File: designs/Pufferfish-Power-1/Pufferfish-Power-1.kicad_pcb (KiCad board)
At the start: 2 copper layers, 9 parts, among them Q1 BSC028N06LS3, Q2 BSC028N06LS3, Q3 BSC028N06LS3, Q4 BSC028N06LS3, U1 LTC4421IUHE

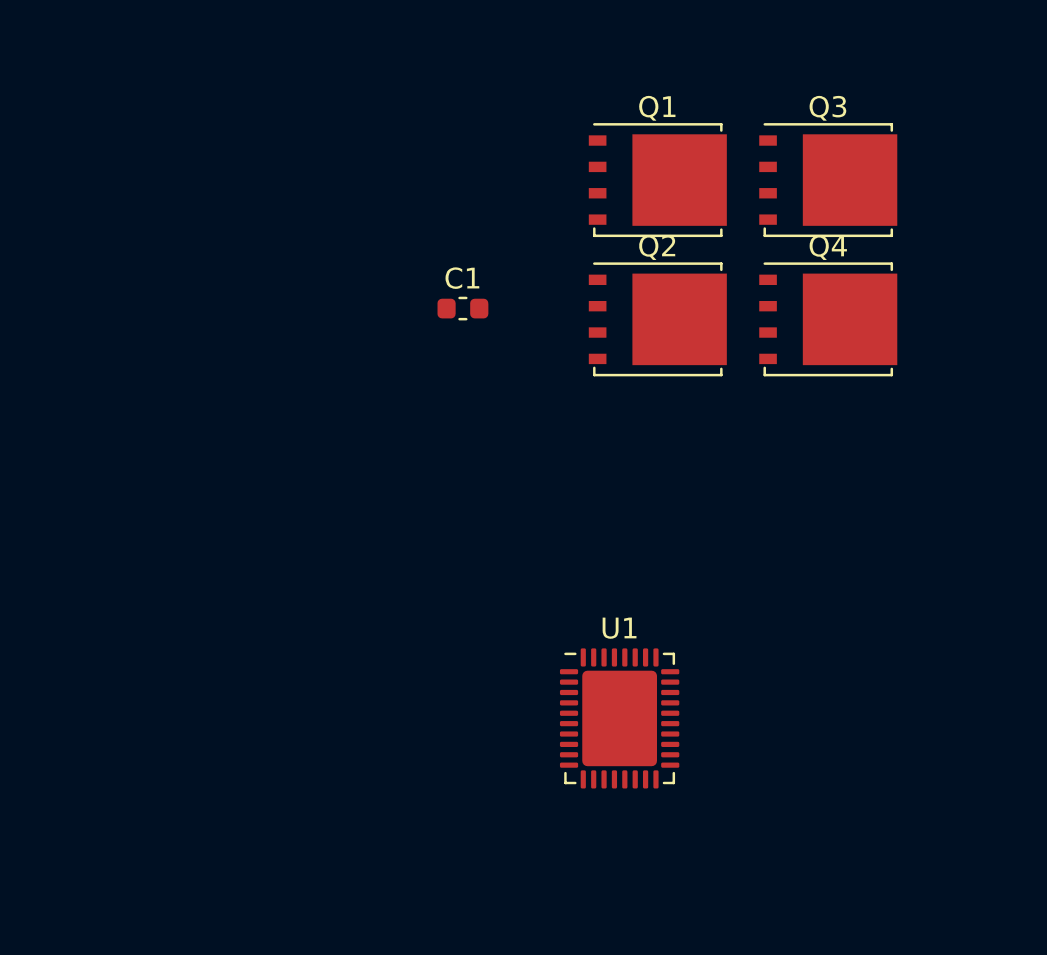
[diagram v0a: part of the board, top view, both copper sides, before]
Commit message: - Updated thresholds for LTC4421 circuit - Added inputs page - Added passives to library
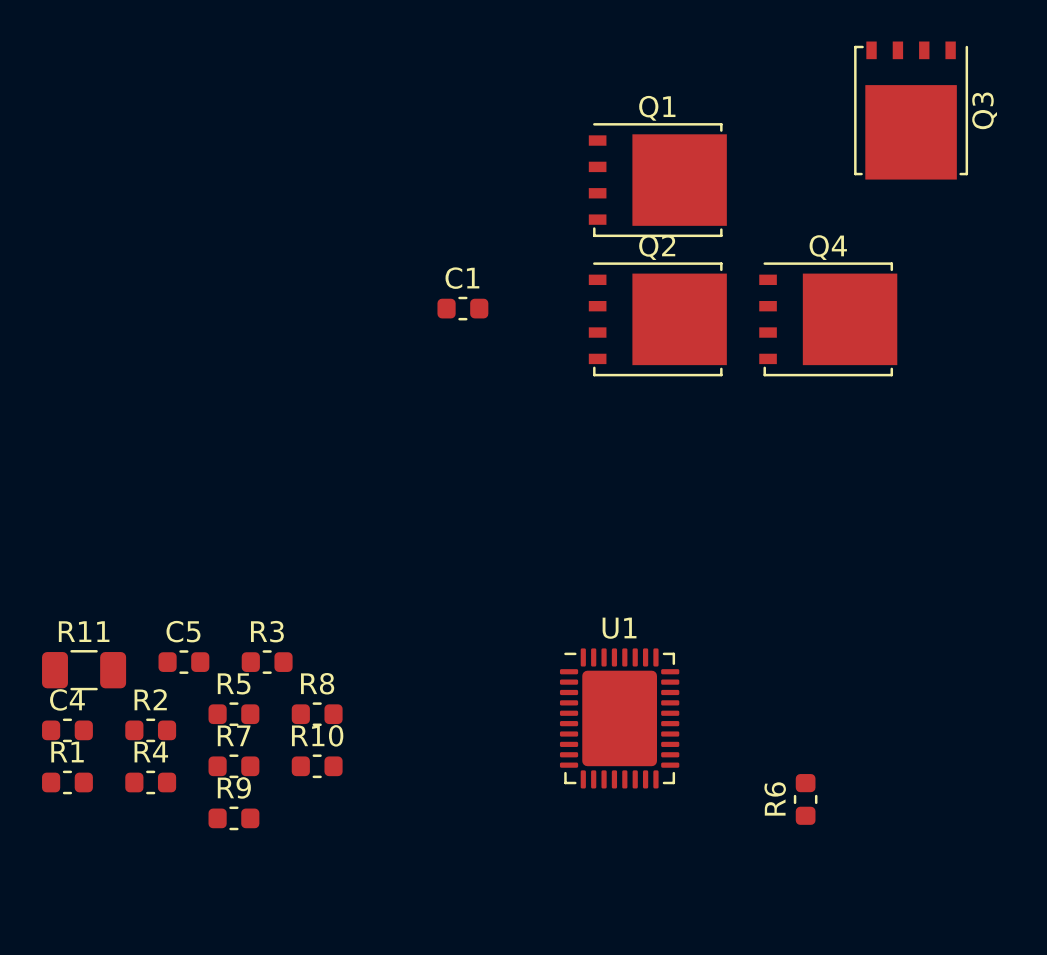
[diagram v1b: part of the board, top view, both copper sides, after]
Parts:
- added C4: CAP_33nF_25V_X7R_0603, Pufferfish:CAP_SMD_0603, F.Cu at (105.4, 114.3)
- added C5: CAP_33nF_25V_X7R_0603, Pufferfish:CAP_SMD_0603, F.Cu at (111.0, 111.0)
- added R1: RES_768K_0603_SMD, Pufferfish:RES_SMD_0603, F.Cu at (105.4, 116.8)
- added R10: RES_47K_0603_SMD, Pufferfish:RES_SMD_0603, F.Cu at (117.4, 116.0)
- added R11: CSNL1206FT3L00, Pufferfish:RES_SMD_1206, F.Cu at (106.2, 111.4)
- added R2: RES_24K9_0603_SMD, Pufferfish:RES_SMD_0603, F.Cu at (109.4, 114.3)
- added R3: RES_750K_0603_SMD, Pufferfish:RES_SMD_0603, F.Cu at (115.0, 111.0)
- added R4: RES_10K_0603_SMD, Pufferfish:RES_SMD_0603, F.Cu at (109.4, 116.8)
- added R5: RES_47K_0603_SMD, Pufferfish:RES_SMD_0603, F.Cu at (113.4, 113.5)
- added R6: RES_768K_0603_SMD, Pufferfish:RES_SMD_0603, F.Cu at (141.0, 117.6)
- added R7: RES_24K9_0603_SMD, Pufferfish:RES_SMD_0603, F.Cu at (113.4, 116.0)
- added R8: RES_750K_0603_SMD, Pufferfish:RES_SMD_0603, F.Cu at (117.4, 113.5)
- added R9: RES_10K_0603_SMD, Pufferfish:RES_SMD_0603, F.Cu at (113.4, 118.5)
- moved Q3 5.21 mm to (146.1, 84.4), turned to 270 degrees
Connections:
- net Net-(Q1-Pad1) renamed VIN-PRIMARY-12V0
- U1 pad 22: Net-(U1-Pad22) -> /LTC4221/LTC4421-TMR2
- U1 pad 23: Net-(U1-Pad23) -> /LTC4221/LTC4421-OV2
- U1 pad 24: Net-(U1-Pad24) -> /LTC4221/LTC4421-UVR2
- U1 pad 25: Net-(U1-Pad25) -> /LTC4221/LTC4421-UVF2
- U1 pad 4: Net-(U1-Pad4) -> /LTC4221/LTC4421-UVF1
- U1 pad 5: Net-(U1-Pad5) -> /LTC4221/LTC4421-UVR1
- U1 pad 6: Net-(U1-Pad6) -> /LTC4221/LTC4421-OV1
- U1 pad 7: Net-(U1-Pad7) -> /LTC4221/LTC4421-TMR1

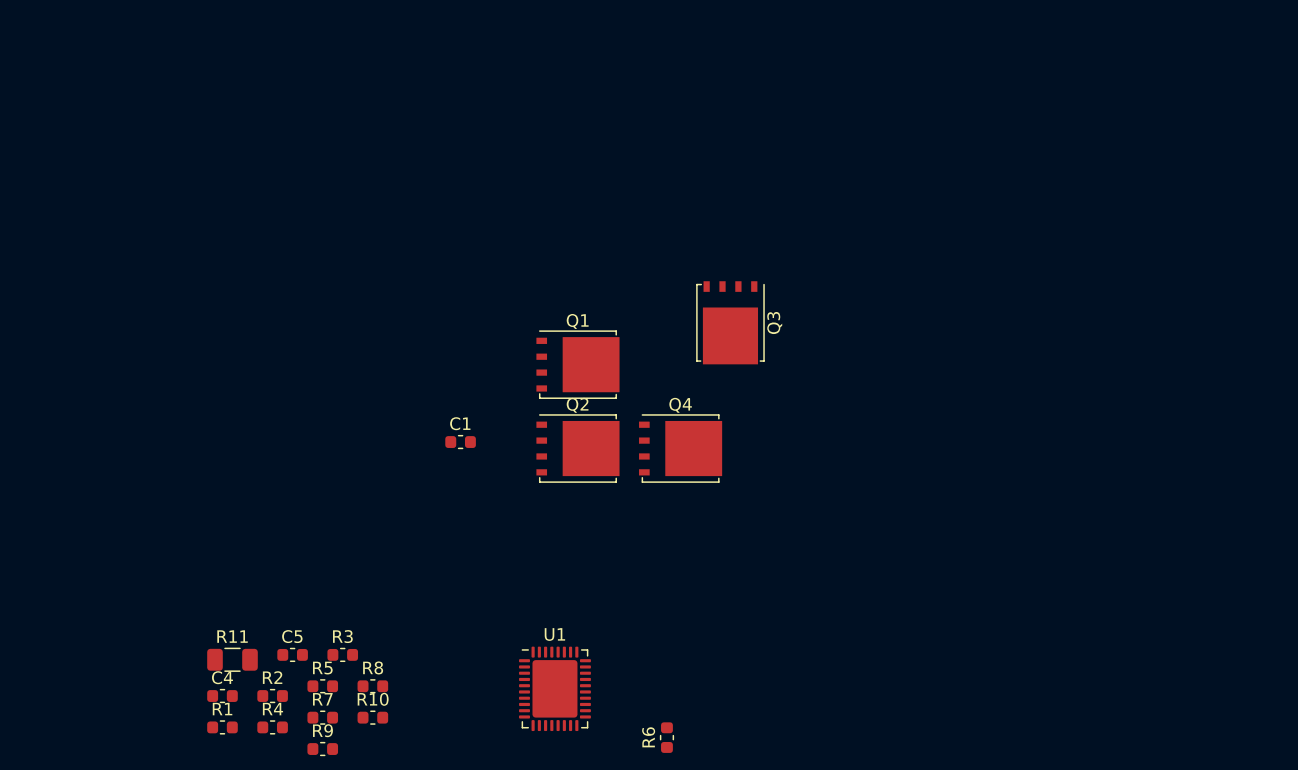
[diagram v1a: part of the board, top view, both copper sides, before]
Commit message: - Finished LTC4421 Design - Added Input power path - Updated libraries - Added pages for interface connectors and 24V Boost
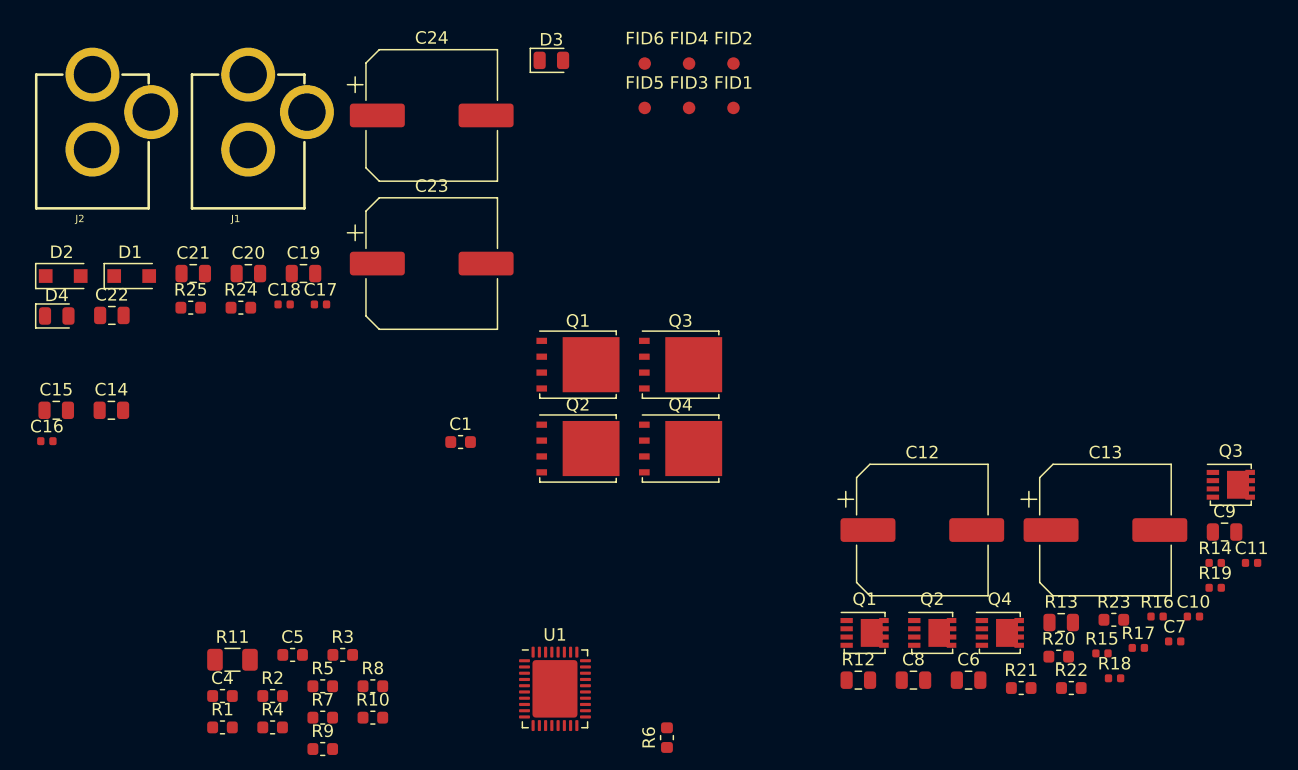
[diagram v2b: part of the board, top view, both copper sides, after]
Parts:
- added C10: CAP_47nF_50V_X7R_0402, Pufferfish:CAP_SMD_0402, F.Cu at (183.1, 107.9)
- added C11: CAP_100nF_50V_X7R_0402, Pufferfish:CAP_SMD_0402, F.Cu at (187.7, 103.7)
- added C12: CAP_AE_SMD_220uF_25V_8mm, Capacitor_SMD:CP_Elec_10x7.9, F.Cu at (161.4, 101.0)
- added C13: CAP_AE_SMD_220uF_25V_8mm, Capacitor_SMD:CP_Elec_10x7.9, F.Cu at (176.1, 101.0)
- added C14: CAP_10uF_35V_X5R_0805, Pufferfish:CAP_SMD_0805, F.Cu at (96.5, 91.4)
- added C15: CAP_10uF_35V_X5R_0805, Pufferfish:CAP_SMD_0805, F.Cu at (92.1, 91.4)
- added C16: CAP_100nF_50V_X7R_0402, Pufferfish:CAP_SMD_0402, F.Cu at (91.4, 93.9)
- added C17: CAP_100nF_50V_X7R_0402, Pufferfish:CAP_SMD_0402, F.Cu at (113.2, 83.0)
- added C18: CAP_100nF_50V_X7R_0402, Pufferfish:CAP_SMD_0402, F.Cu at (110.3, 83.0)
- added C19: CAP_10uF_35V_X5R_0805, Pufferfish:CAP_SMD_0805, F.Cu at (111.9, 80.5)
- added C20: CAP_10uF_35V_X5R_0805, Pufferfish:CAP_SMD_0805, F.Cu at (107.5, 80.5)
- added C21: CAP_10uF_35V_X5R_0805, Pufferfish:CAP_SMD_0805, F.Cu at (103.1, 80.5)
- added C22: CAP_10uF_35V_X5R_0805, Pufferfish:CAP_SMD_0805, F.Cu at (96.6, 83.8)
- added C23: CAP_AE_SMD_220uF_25V_8mm, Capacitor_SMD:CP_Elec_10x7.9, F.Cu at (122.2, 79.7)
- added C24: CAP_AE_SMD_220uF_25V_8mm, Capacitor_SMD:CP_Elec_10x7.9, F.Cu at (122.2, 67.8)
- added C6: CAP_10uF_35V_X5R_0805, Pufferfish:CAP_SMD_0805, F.Cu at (165.1, 113.0)
- added C7: CAP_47nF_50V_X7R_0402, Pufferfish:CAP_SMD_0402, F.Cu at (181.6, 109.9)
- added C8: CAP_10uF_35V_X5R_0805, Pufferfish:CAP_SMD_0805, F.Cu at (160.7, 113.0)
- added C9: CAP_10uF_35V_X5R_0805, Pufferfish:CAP_SMD_0805, F.Cu at (185.6, 101.2)
- added D1: TVS_15V_SOD123FL-2, Diode_SMD:D_SOD-123F, F.Cu at (98.1, 80.7)
- added D2: TVS_15V_SOD123FL-2, Diode_SMD:D_SOD-123F, F.Cu at (92.7, 80.7)
- added D3: LED_SMD_0805, Pufferfish:LED_SMD_0805, F.Cu at (131.7, 63.4)
- added D4: LED_SMD_0805, Pufferfish:LED_SMD_0805, F.Cu at (92.2, 83.9)
- added FID1: Fiducial, Fiducial:Fiducial_1mm_Mask2mm, F.Cu at (146.3, 67.2)
- added FID2: Fiducial, Fiducial:Fiducial_1mm_Mask2mm, F.Cu at (146.3, 63.7)
- added FID3: Fiducial, Fiducial:Fiducial_1mm_Mask2mm, F.Cu at (142.7, 67.2)
- added FID4: Fiducial, Fiducial:Fiducial_1mm_Mask2mm, F.Cu at (142.7, 63.7)
- added FID5: Fiducial, Fiducial:Fiducial_1mm_Mask2mm, F.Cu at (139.2, 67.2)
- added FID6: Fiducial, Fiducial:Fiducial_1mm_Mask2mm, F.Cu at (139.2, 63.7)
- added J1: POWER_JACK_PTH, Pufferfish:POWER_JACK_PTH, F.Cu at (107.5, 78.3)
- added J2: POWER_JACK_PTH, Pufferfish:POWER_JACK_PTH, F.Cu at (95.0, 78.3)
- added Q1: SiR158DP, Package_SO:Vishay_PowerPAK_1212-8_Single, F.Cu at (156.8, 109.2)
- added Q2: SiR158DP, Package_SO:Vishay_PowerPAK_1212-8_Single, F.Cu at (162.2, 109.2)
- added Q3: SiR158DP, Package_SO:Vishay_PowerPAK_1212-8_Single, F.Cu at (186.1, 97.4)
- added Q4: SiR158DP, Package_SO:Vishay_PowerPAK_1212-8_Single, F.Cu at (167.6, 109.2)
- added R12: RES_1R2_0805_SMD, Pufferfish:RES_SMD_0805, F.Cu at (156.3, 113.0)
- added R13: RES_1R2_0805_SMD, Pufferfish:RES_SMD_0805, F.Cu at (172.5, 108.4)
- added R14: RES_0R_0402_SMD, Pufferfish:RES_SMD_0402, F.Cu at (184.8, 103.7)
- added R15: RES_0R_0402_SMD, Pufferfish:RES_SMD_0402, F.Cu at (175.8, 110.9)
- added R16: RES_0R_0402_SMD, Pufferfish:RES_SMD_0402, F.Cu at (180.2, 107.9)
- added R17: RES_0R_0402_SMD, Pufferfish:RES_SMD_0402, F.Cu at (178.7, 110.5)
- added R18: RES_0R_0402_SMD, Pufferfish:RES_SMD_0402, F.Cu at (176.8, 112.9)
- added R19: RES_0R_0402_SMD, Pufferfish:RES_SMD_0402, F.Cu at (184.8, 105.6)
- added R20: RES_10K_0603_SMD, Pufferfish:RES_SMD_0603, F.Cu at (172.3, 111.2)
- added R21: RES_10K_0603_SMD, Pufferfish:RES_SMD_0603, F.Cu at (169.3, 113.7)
- added R22: RES_10K_0603_SMD, Pufferfish:RES_SMD_0603, F.Cu at (173.3, 113.7)
- added R23: RES_10K_0603_SMD, Pufferfish:RES_SMD_0603, F.Cu at (176.7, 108.2)
- added R24: RES_330R_0603_SMD, Pufferfish:RES_SMD_0603, F.Cu at (106.9, 83.2)
- added R25: RES_330R_0603_SMD, Pufferfish:RES_SMD_0603, F.Cu at (102.9, 83.2)
- moved Q3 5.21 mm to (142.1, 87.8), turned to 0 degrees
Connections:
- R11 pad 1: Net-(R11-Pad1) -> VSYS-12V0
- R11 pad 2: Net-(R11-Pad2) -> /LTC4221/LTC4421-SENSE
- U1 pad 1: Net-(U1-Pad1) -> /LTC4221/LTC4421-SRC1
- U1 pad 17: Net-(U1-Pad17) -> INTVCC-LTC4421
- U1 pad 2: Net-(U1-Pad2) -> /LTC4221/LTC4421-GATE1
- U1 pad 21: Net-(U1-Pad21) -> LTC4421-PWR-nDISABLE2
- U1 pad 26: Net-(U1-Pad26) -> VIN-BACKUP-12V0
- U1 pad 27: Net-(U1-Pad27) -> /LTC4221/LTC4421-SOURCE2
- U1 pad 28: Net-(U1-Pad28) -> /LTC4221/LTC4421-GATE2
- U1 pad 29: Net-(U1-Pad29) -> /LTC4221/LTC4421-SENSE
- U1 pad 3: Net-(U1-Pad3) -> VIN-PRIMARY-12V0
- U1 pad 30: Net-(U1-Pad30) -> VSYS-12V0
- U1 pad 32: Net-(U1-Pad32) -> VSYS-12V0
- U1 pad 33: Net-(U1-Pad33) -> VSYS-12V0
- U1 pad 34: Net-(U1-Pad34) -> VSYS-12V0
- U1 pad 35: Net-(U1-Pad35) -> VSYS-12V0
- U1 pad 36: Net-(U1-Pad36) -> /LTC4221/LTC4421-SENSE
- U1 pad 8: Net-(U1-Pad8) -> LTC4421-PWR-nDISABLE1

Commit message: - Added 3.3V and 5V Buck designs - Added interface connectors - Added voltage measurement circuit - Added preliminary charging circuit
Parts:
- added C25: CAP_22uF_25V_X5R_0805, Pufferfish:CAP_SMD_0805, F.Cu at (135.9, 38.1)
- added C26: CAP_22uF_25V_X5R_0805, Pufferfish:CAP_SMD_0805, F.Cu at (131.4, 42.6)
- added C27: CAP_22uF_25V_X5R_0805, Pufferfish:CAP_SMD_0805, F.Cu at (135.8, 44.0)
- added C28: CAP_22uF_25V_X5R_0805, Pufferfish:CAP_SMD_0805, F.Cu at (140.3, 38.1)
- added C29: CAP_22uF_25V_X5R_0805, Pufferfish:CAP_SMD_0805, F.Cu at (135.9, 41.0)
- added C30: CAP_22uF_25V_X5R_0805, Pufferfish:CAP_SMD_0805, F.Cu at (131.4, 45.6)
- added C31: CAP_22uF_25V_X5R_0805, Pufferfish:CAP_SMD_0805, F.Cu at (136.7, 24.0)
- added C32: CAP_22uF_25V_X5R_0805, Pufferfish:CAP_SMD_0805, F.Cu at (126.0, 29.2)
- added C33: CAP_22uF_25V_X5R_0805, Pufferfish:CAP_SMD_0805, F.Cu at (141.1, 21.0)
- added C34: CAP_10uF_35V_X5R_0805, Pufferfish:CAP_SMD_0805, F.Cu at (130.4, 32.1)
- added C35: CAP_4.7uF_16V_X6S_0603, Pufferfish:CAP_SMD_0603, F.Cu at (140.9, 23.8)
- added C36: CAP_100nF_50V_X7R_0402, Pufferfish:CAP_SMD_0402, F.Cu at (142.1, 26.0)
- added C37: CAP_100nF_50V_X7R_0402, Pufferfish:CAP_SMD_0402, F.Cu at (142.1, 28.0)
- added C38: CAP_47nF_50V_X7R_0402, Pufferfish:CAP_SMD_0402, F.Cu at (145.0, 26.0)
- added C39: CAP_1nF_50V_C0G_0402, Pufferfish:CAP_SMD_0402, F.Cu at (141.0, 30.0)
- added C40: CAP_100nF_50V_X7R_0402, Pufferfish:CAP_SMD_0402, F.Cu at (145.0, 28.0)
- added C41: CAP_100pF_10V_NP0_0402, Pufferfish:CAP_SMD_0402, F.Cu at (141.0, 32.0)
- added C42: CAP_22uF_25V_X5R_0805, Pufferfish:CAP_SMD_0805, F.Cu at (130.4, 29.2)
- added C43: CAP_22uF_25V_X5R_0805, Pufferfish:CAP_SMD_0805, F.Cu at (126.0, 32.1)
- added C44: CAP_22uF_25V_X5R_0805, Pufferfish:CAP_SMD_0805, F.Cu at (136.7, 21.0)
- added C45: CAP_AE_SMD_100uF_10V_6mm, Capacitor_SMD:CP_Elec_6.3x5.4, F.Cu at (129.2, 23.6)
- added C46: CAP_22uF_25V_X5R_0805, Pufferfish:CAP_SMD_0805, F.Cu at (68.0, 60.4)
- added C47: CAP_22uF_25V_X5R_0805, Pufferfish:CAP_SMD_0805, F.Cu at (72.5, 57.5)
- added C48: CAP_3.3nF_50V_X7R_0402, Pufferfish:CAP_SMD_0402, F.Cu at (62.9, 65.8)
- added C49: CAP_22uF_25V_X5R_0805, Pufferfish:CAP_SMD_0805, F.Cu at (63.6, 57.5)
- added C50: CAP_1nF_50V_C0G_0402, Pufferfish:CAP_SMD_0402, F.Cu at (75.7, 59.9)
- added C51: CAP_100pF_10V_NP0_0402, Pufferfish:CAP_SMD_0402, F.Cu at (71.3, 65.4)
- added C52: CAP_22uF_25V_X5R_0805, Pufferfish:CAP_SMD_0805, F.Cu at (63.6, 60.4)
- added C53: CAP_22uF_25V_X5R_0805, Pufferfish:CAP_SMD_0805, F.Cu at (68.0, 57.5)
- added C54: CAP_22uF_25V_X5R_0805, Pufferfish:CAP_SMD_0805, F.Cu at (63.6, 63.4)
- added C55: CAP_1uF_35V_X7R_0603, Pufferfish:CAP_SMD_0603, F.Cu at (193.0, 35.6)
- added J3: Molex_PicoFlex_20_Vertical, Connector_Molex:Molex_Picoflex_90325-0020_2x10_P1.27mm_Vertical, F.Cu at (250.2, 100.3)
- added J4: Molex_MicroFit3_2x4_Receptacle, Connector_Molex:Molex_Micro-Fit_3.0_43045-0800_2x04_P3.00mm_Horizontal, F.Cu at (250.9, 55.4)
- added Q5: 2N7002E, Package_TO_SOT_SMD:SOT-23, F.Cu at (131.5, 38.9)
- added Q6: SiSS27DN, Package_SO:Vishay_PowerPAK_1212-8_Single, F.Cu at (126.5, 38.9)
- added Q7: SiSS27DN, Package_SO:Vishay_PowerPAK_1212-8_Single, F.Cu at (126.5, 43.5)
- added Q8: TP0610T, Package_TO_SOT_SMD:SOT-23, F.Cu at (188.8, 36.6)
- added Q9: 2N7002E, Package_TO_SOT_SMD:SOT-23, F.Cu at (188.8, 41.1)
- added R26: RES_10K_0603_SMD, Pufferfish:RES_SMD_0603, F.Cu at (140.1, 40.8)
- added R27: RES_100K_0603_SMD, Pufferfish:RES_SMD_0603, F.Cu at (140.1, 43.8)
- added R28: RES_62K_0402_SMD, Pufferfish:RES_SMD_0402, F.Cu at (138.1, 31.0)
- added R29: RES_51K_0402_SMD, Pufferfish:RES_SMD_0402, F.Cu at (138.1, 29.0)
- added R30: RES_47K_0603_SMD, Pufferfish:RES_SMD_0603, F.Cu at (145.3, 20.8)
- added R31: RES_10K_0603_SMD, Pufferfish:RES_SMD_0603, F.Cu at (134.7, 31.5)
- added R32: RES_0R_0402_SMD, Pufferfish:RES_SMD_0402, F.Cu at (143.9, 30.0)
- added R33: RES_10K_0603_SMD, Pufferfish:RES_SMD_0603, F.Cu at (138.7, 26.7)
- added R34: RES_10K_0603_SMD, Pufferfish:RES_SMD_0603, F.Cu at (134.7, 29.0)
- added R35: RES_73K2_0603_SMD, Pufferfish:RES_SMD_0603, F.Cu at (144.9, 23.8)
- added R36: RES_73K2_0603_SMD, Pufferfish:RES_SMD_0603, F.Cu at (72.3, 60.2)
- added R37: RES_10K_0603_SMD, Pufferfish:RES_SMD_0603, F.Cu at (76.7, 57.2)
- added R38: RES_10K_0603_SMD, Pufferfish:RES_SMD_0603, F.Cu at (67.8, 65.7)
- added R39: RES_31K6_0603_SMD, Pufferfish:RES_SMD_0603, F.Cu at (71.9, 63.1)
- added R40: RES_10K_0603_SMD, Pufferfish:RES_SMD_0603, F.Cu at (67.8, 63.1)
- added R41: RES_10K_0603_SMD, Pufferfish:RES_SMD_0603, F.Cu at (188.6, 44.7)
- added R42: RES_10K_0603_SMD, Pufferfish:RES_SMD_0603, F.Cu at (197.1, 35.6)
- added R43: RES_47K_0603_SMD, Pufferfish:RES_SMD_0603, F.Cu at (193.0, 38.1)
- added R44: RES_10K_0603_SMD, Pufferfish:RES_SMD_0603, F.Cu at (197.1, 38.1)
- added R45: RES_10K_0603_SMD, Pufferfish:RES_SMD_0603, F.Cu at (193.0, 40.6)
- added R46: RES_10K_0603_SMD, Pufferfish:RES_SMD_0603, F.Cu at (192.6, 44.7)
- added R47: RES_10K_0603_SMD, Pufferfish:RES_SMD_0603, F.Cu at (201.1, 35.6)
- added R48: RES_10K_0603_SMD, Pufferfish:RES_SMD_0603, F.Cu at (197.1, 40.6)
- added R49: RES_10K_0603_SMD, Pufferfish:RES_SMD_0603, F.Cu at (201.1, 38.1)
- added R50: RES_10K_0603_SMD, Pufferfish:RES_SMD_0603, F.Cu at (196.6, 43.1)
- added R51: RES_10K_0603_SMD, Pufferfish:RES_SMD_0603, F.Cu at (205.1, 35.6)
- added R52: RES_10K_0603_SMD, Pufferfish:RES_SMD_0603, F.Cu at (201.1, 40.6)
- added U2: TPS568215RNN, Package_DFN_QFN:Texas_RNN0018A, F.Cu at (174.0, 74.9)
- added U3: TPS82130, Package_LGA:Texas_SIL0008D_MicroSiP-8-1EP_2.8x3mm_P0.65mm_EP1.1x1.9mm_ThermalVias, F.Cu at (199.4, 77.5)
